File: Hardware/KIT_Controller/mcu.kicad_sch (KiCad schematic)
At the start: 27 parts, among them J201 USB_B, J202 USB_BOOT, U202 W25Q128JVS, U203 NCP1117-3.3_SOT223, U205 RP2040, Y201 Crystal

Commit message: Add gnd and cleanup
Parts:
- removed J201: USB_B, Connector_USB:USB_B_OST_USB-B1HSxx_Horizontal, symbol Connector:USB_B
- added J203: USBC, Connector_USB:USB_C_Receptacle_XKB_U262-16XN-4BVC11, symbol Connector:USB_C_Receptacle_USB2.0
- added R206, R207: 5K1, Resistor_SMD:R_0805_2012Metric, symbol Device:R_Small
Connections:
- net GND: now also J203.A1 (GND), J203.A12 (GND), J203.B1 (GND), J203.B12 (GND), J203.S1 (SHIELD), R206.1, R207.1
- net VBUS: now also J203.A4 (VBUS), J203.A9 (VBUS), J203.B4 (VBUS), J203.B9 (VBUS)
- new net: J203.B5 (CC2), R206.2
- new net: J203.A5 (CC1), R207.2
- new net USB+: J203.A6 (D+), J203.B6 (D+)
- new net USB-: J203.A7 (D-), J203.B7 (D-)
- no-connect marks 28 -> 30
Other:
- moved on the sheet: C203, C205, U203

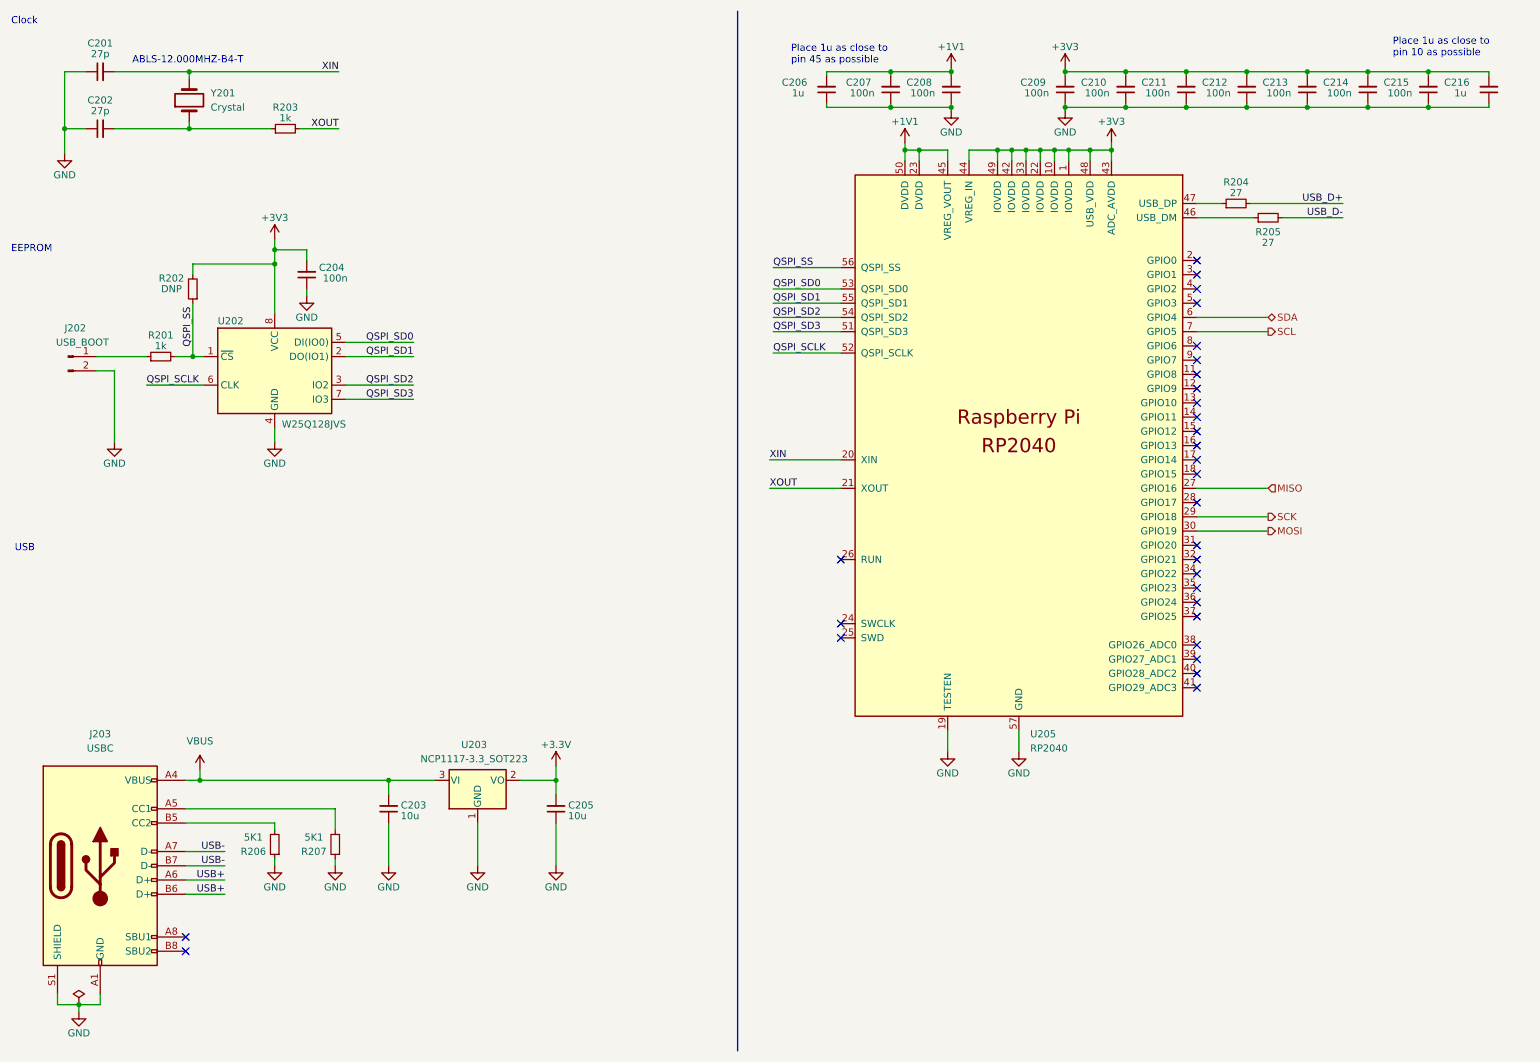
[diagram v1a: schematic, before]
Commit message: Add SD cardg
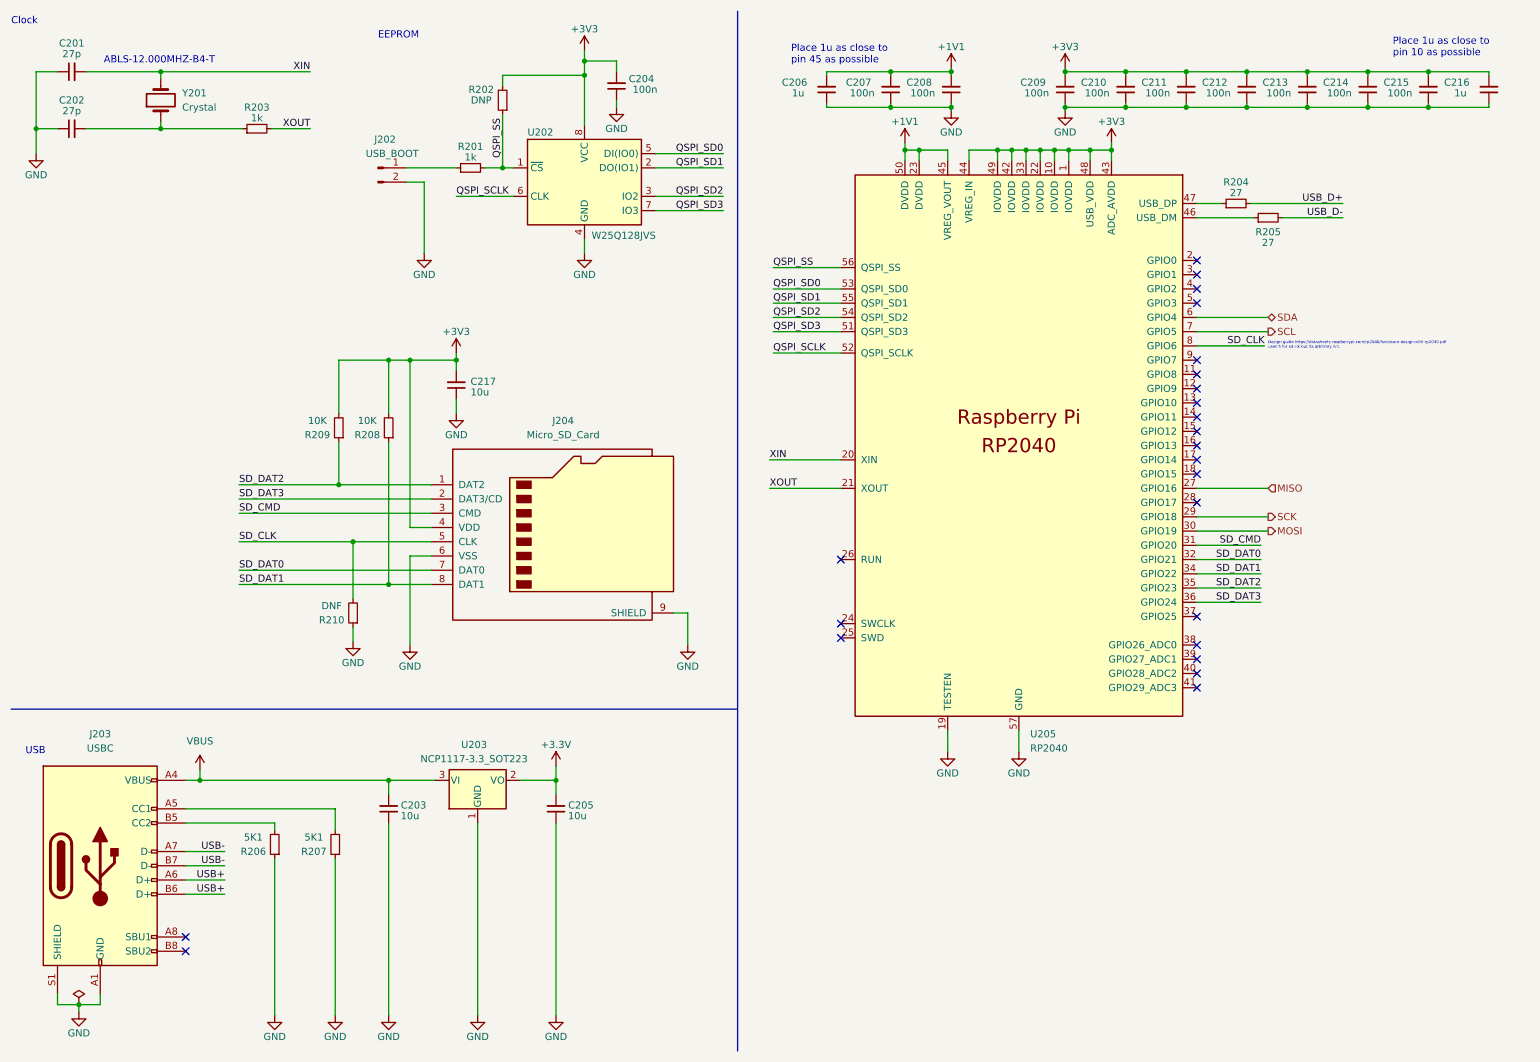
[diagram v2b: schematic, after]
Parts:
- added C217: 10u, Capacitor_SMD:C_0805_2012Metric, symbol Device:C_Small
- added J204: Micro_SD_Card, Connector_Card:microSD_HC_Molex_47219-2001, symbol Connector:Micro_SD_Card
- added R208, R209: 10K, Resistor_SMD:R_0805_2012Metric, symbol Device:R_Small
- added R210: DNF, Resistor_SMD:R_0805_2012Metric, symbol Device:R_Small
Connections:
- net +3V3: now also C217.2, J204.4 (VDD), R208.2, R209.2
- net GND: now also C217.1, J204.6 (VSS), J204.9 (SHIELD), R210.1
- net SD_CMD: now reaches U205.31 (GPIO20)
- net SD_CMD: now also J204.3 (CMD)
- net SD_DAT0: now reaches U205.32 (GPIO21)
- net SD_DAT0: now also J204.7 (DAT0)
- net SD_DAT1: now reaches U205.34 (GPIO22)
- net SD_DAT1: now also J204.8 (DAT1), R208.1
- net SD_DAT2: now reaches U205.35 (GPIO23)
- net SD_DAT2: now also J204.1 (DAT2), R209.1
- net SD_DAT3: now reaches U205.36 (GPIO24)
- net SD_DAT3: now also J204.2 (DAT3/CD)
- net SD_CLK: now reaches U205.8 (GPIO6)
- net SD_CLK: now also J204.5 (CLK), R210.2
- no-connect marks 30 -> 24
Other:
- note added: "Design guide https://datasheets.raspberrypi.com/rp2040/hardware-design-with-rp2040.pdf uses 5 for sd clk but its arbitrary iirc."
- moved on the sheet: C201, C202, C204, J202, R201, R202, R203, U202, Y201

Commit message: Add stuff
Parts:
- removed J204: Micro_SD_Card, Connector_Card:microSD_HC_Molex_47219-2001, symbol Connector:Micro_SD_Card
- added J3: Micro_SD_Card_Det1, Connector_Card:microSD_HC_Molex_104031-0811, symbol Connector:Micro_SD_Card_Det1
- added R215, R216, R217: DNP, Resistor_SMD:R_0805_2012Metric, symbol Device:R_Small
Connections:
- net +3V3: now also J3.4 (VDD), R215.2, R216.2, R217.2
- net GND: now also J3.10 (SHIELD), J3.6 (VSS)
- net SD_CLK: now also J3.5 (CLK), R217.1
- net SD_CMD: now also J3.3 (CMD)
- net SD_DAT0: now also J3.7 (DAT0), R216.1
- net SD_DAT1: now also J3.8 (DAT1)
- net SD_DAT2: now also J3.1 (DAT2)
- net SD_DAT3: now also J3.2 (DAT3/CD), R215.1
- no-connect marks 24 -> 25
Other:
- note added: "CLK?"
- note added: "MISO?"
- note added: "MOSI?"
- note added: "More SD Card research needs to be done!"
- note added: "What for?"
